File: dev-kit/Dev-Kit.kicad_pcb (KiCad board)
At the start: 4 copper layers, 105 x 70 mm, 110 parts, among them IC101 nPM1300-QEXX, IC107 USBLC6-2P6, IC201 APDS-9306-065, IC202 BMI270, IC203 BMP581, IC204 LIS2MDLTR, IC302 FAN5622SX, IC303 MX25U51245GZ4I00, IC305 NTS0104GU12, IC306 DRV2603RUNT, IC307 RV-8263-C8, M301 NORA-B106, Q201 DMG1013UW-7, Q301 BC817W, Q302 PMZ550UNEYL, Q303 PMZ550UNEYL, U201 MAX98357A, X101 Battery, X102 Motor, X103 Device, X104 DEBUG, X201 Power, X202 Power, X203 Power, X204 Power, X205 Power, X206 Power, X207 Power, X208 Power, X209 LED Power, X210 Touch Power, X211 IO Power, X302 Display

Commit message: Add CI/CD pipeline for Dev-Kit, more Dev-Kit improvements
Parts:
- removed BZ301: Buzzer, CUI Devices:CMT-322-65-SMT-TR
- removed D301: BAS316, Diode_SMD:D_SOD-323
- removed Q301: BC817W, Package_TO_SOT_SMD:SOT-323_SC-70
- removed R121: 0R, Resistor_SMD:R_0805_2012Metric
- removed R307: 150k, Resistor_SMD:R_0603_1608Metric
- removed R311: 180R, Resistor_SMD:R_0603_1608Metric
- removed TP104: SDA, TestPoint:TestPoint_Pad_D1.0mm
- removed TP105: SCL, TestPoint:TestPoint_Pad_D1.0mm
- removed U201: MAX98357A, Package_DFN_QFN:TQFN-16-1EP_3x3mm_P0.5mm_EP1.23x1.23mm
- added G***: LOGO, footprints:Logo, F.Cu at (156.8, 120.7)
- added X212: Power, Connector_PinHeader_2.54mm:PinHeader_1x02_P2.54mm_Vertical_SMD_Pin1Left, F.Cu at (158.0, 82.4)
- added X213: I2C, Connector_PinHeader_2.54mm:PinHeader_1x04_P2.54mm_Vertical_SMD_Pin1Left, F.Cu at (151.6, 139.2)
- added X214: I2S, Connector_PinHeader_2.54mm:PinHeader_1x05_P2.54mm_Vertical_SMD_Pin1Left, F.Cu at (139.7, 138.0)
- moved S301 60.8 mm to (148.0, 83.0), turned to 0 degrees
- moved S302 56.6 mm to (148.0, 128.0), turned to 0 degrees
- moved S304 53.2 mm to (123.0, 83.0), turned to 0 degrees
- moved X209 40.6 mm to (154.4, 112.7), turned to -90 degrees
- moved X210 39.0 mm to (152.2, 92.1)
- moved X211 38.9 mm to (158.6, 92.1), turned to -90 degrees
- moved S303 31.1 mm to (123.0, 129.0), turned to 0 degrees
- moved C301 29.3 mm to (165.1, 107.5)
- moved R301 29.3 mm to (165.1, 108.5)
- moved IC302 29.3 mm to (162.6, 108.1)
- moved R126 29.3 mm to (164.6, 105.1)
- moved R117 26.5 mm to (161.2, 101.2)
- moved R118 26.5 mm to (157.3, 101.2)
- moved C304 26.5 mm to (160.5, 99.7)
- moved C305 26.5 mm to (158.1, 99.7)
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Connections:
- M301 pad F7: unconnected-(M301C-P1.07-PadF7) -> /MCU/MCLK
- M301 pad G1: /MCU/SW3 -> /MCU/SW2
- M301 pad G2: /MCU/SW2 -> /MCU/SW4
- M301 pad G7: unconnected-(M301C-P1.09-PadG7) -> /MCU/WS
- M301 pad H1: /MCU/SW4 -> /MCU/SW3
- M301 pad J7: unconnected-(M301C-P1.10-PadJ7) -> /MCU/Data
- X211 pad 1: Net-(X211-Pin_1) -> +1V8
- X211 pad 2: +1V8 -> Net-(X211-Pin_2)
- X302 pad 11: Net-(X211-Pin_1) -> Net-(X211-Pin_2)
- X302 pad 12: Net-(X211-Pin_1) -> Net-(X211-Pin_2)
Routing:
- net /MCU/WS: track 0.00 -> 90.1 mm, vias 0 -> 3
- net /MCU/Data: track 0.00 -> 89.7 mm, vias 0 -> 3
- net /MCU/MCLK: track 0.00 -> 81.6 mm, vias 0 -> 3
- net /MCU/SW4: track 106.7 -> 151.3 mm, vias 1 -> 2
- net Net-(X211-Pin_2): track 0.00 -> 44.5 mm
- net Net-(X210-Pin_2): track 10.4 -> 48.9 mm
- net Net-(X209-Pin_2): track 3.24 -> 40.5 mm
- net /MCU/SW2: track 104.3 -> 72.1 mm, vias 1 -> 2
- net LEDK2: track 14.3 -> 43.5 mm
- net LEDK1: track 12.8 -> 42.1 mm
- net DISPLAY-BLK: track 76.2 -> 46.9 mm
- net TOUCH-RST: track 78.7 -> 51.8 mm
- net TOUCH-SDA: track 78.6 -> 51.8 mm
- net TOUCH-SCL: track 78.5 -> 51.9 mm
- net Net-(IC305-B4): track 17.8 -> 44.3 mm
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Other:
- board text added: "+"
- board text added: "-"
- board text added: "Display"

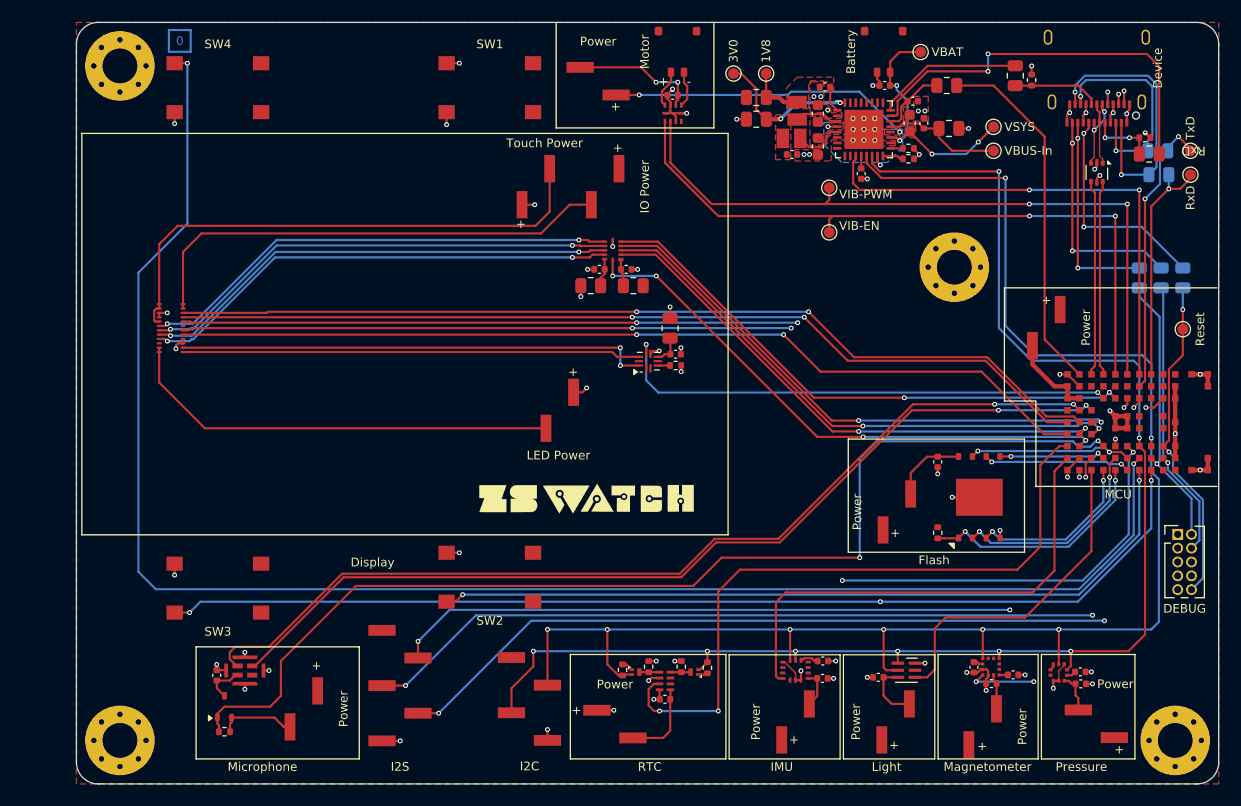
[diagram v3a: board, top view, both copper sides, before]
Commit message: PCB: Tweak silkscreen and headers.
- Added silkscreen labels to headers.
- Added function text to buttons.
- Made PCB 5mm wider (left) to make space for display (not sticking out of PCB) and allow more centered
buttons placement.
- Add header for UART pins (good in case we don't have a working dock built) (no mount).
- Changed from TP to header for VBAT for alternative way to connect battery (no mount).
- Added website url on silkscreen.
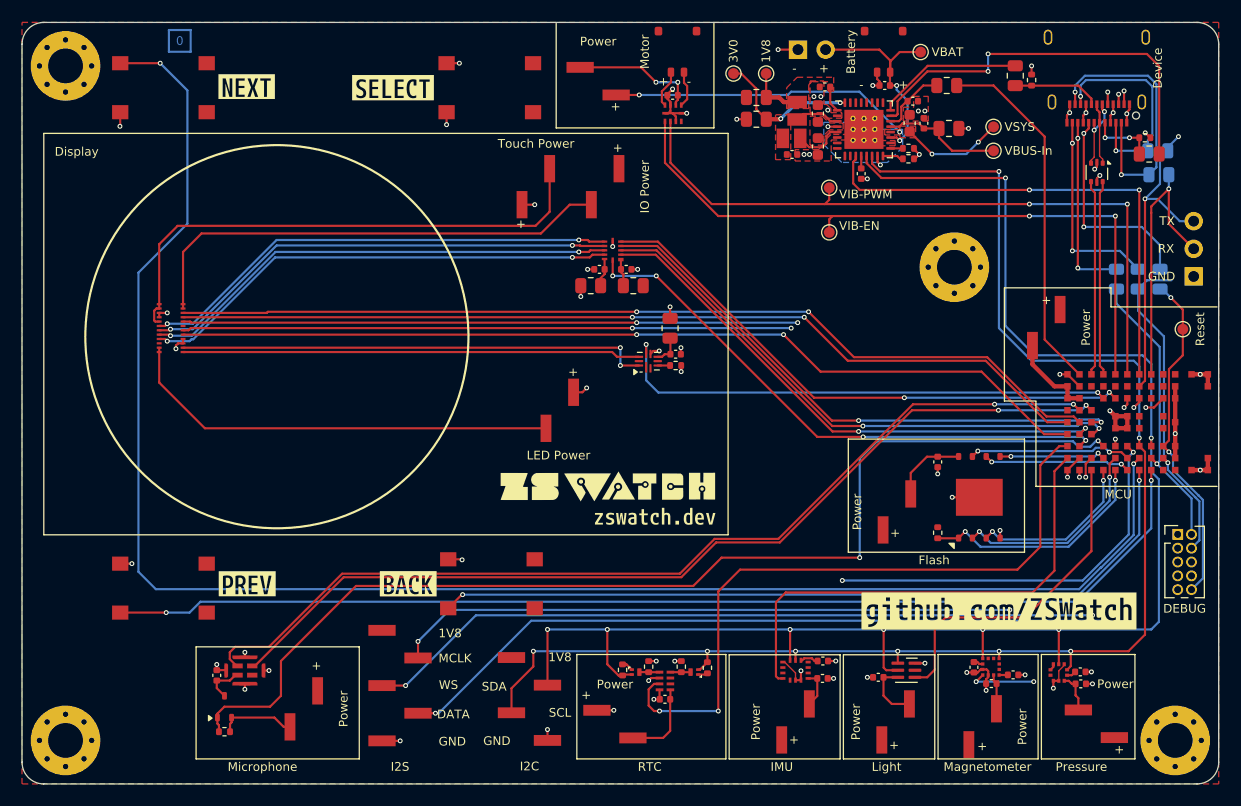
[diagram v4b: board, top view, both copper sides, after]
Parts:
- removed TP108: TxD, TestPoint:TestPoint_Pad_D1.0mm
- removed TP109: RxD, TestPoint:TestPoint_Pad_D1.0mm
- added J1: UART, Connector_PinHeader_2.54mm:PinHeader_1x03_P2.54mm_Vertical, F.Cu at (212.7, 95.3)
- added X1: Battery, Connector_PinHeader_2.54mm:PinHeader_1x02_P2.54mm_Vertical, F.Cu at (176.3, 79.5)
- added kibuzzard-68303879: G***, kibuzzard-68303879, F.Cu at (194.8, 131.1)
- added kibuzzard-68304278: G***, kibuzzard-68304278, F.Cu at (125.7, 128.6)
- added kibuzzard-68304289: G***, kibuzzard-68304289, F.Cu at (140.5, 128.6)
- added kibuzzard-6830428E: G***, kibuzzard-6830428E, F.Cu at (139.1, 83.0)
- added kibuzzard-68304292: G***, kibuzzard-68304292, F.Cu at (125.7, 82.9)
- added kibuzzard-68304463: G***, kibuzzard-68304463, F.Cu at (163.2, 122.4)
- moved REF** 5.00 mm to (109.0, 81.0)
- moved REF** 5.00 mm to (109.0, 143.0)
- moved S303 5.00 mm to (118.0, 129.0)
- moved S304 5.00 mm to (118.0, 83.0)
- moved G*** 2.26 mm to (158.8, 119.6)
- moved R106 2.10 mm to (205.6, 100.6)
- moved R107 2.10 mm to (207.6, 100.6)
- moved R130 2.10 mm to (209.6, 100.6)
- moved S302 0.62 mm to (148.2, 128.6)
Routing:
- net /Peripherals/VBAT: track 15.6 -> 23.0 mm
- net /MCU/SW3: track 139.4 -> 144.4 mm
- net SWDCLK: track 26.3 -> 31.0 mm
- net RxD: track 22.1 -> 25.8 mm
- net TxD: track 26.2 -> 29.9 mm
- net /MCU/SW4: track 151.3 -> 154.8 mm
- net GND: track 74.5 -> 76.7 mm, vias 57 -> 58
- net Net-(X103-RX1+): track 38.2 -> 36.1 mm
- net Net-(X103-RX1-): track 35.0 -> 33.0 mm
- net Net-(X103-SBU1): track 34.8 -> 34.0 mm
- net SWDIO: track 25.6 -> 26.3 mm
- net RESETn: track 30.4 -> 31.1 mm
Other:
- board size 105 x 70 mm -> 110 x 70 mm
- board text added: "1V8"
- board text added: "DATA"
- board text added: "GND"
- board text added: "MCLK"
- board text added: "RX"
- board text added: "SCL"
- board text added: "SDA"
- board text added: "TX"
- board text added: "WS"

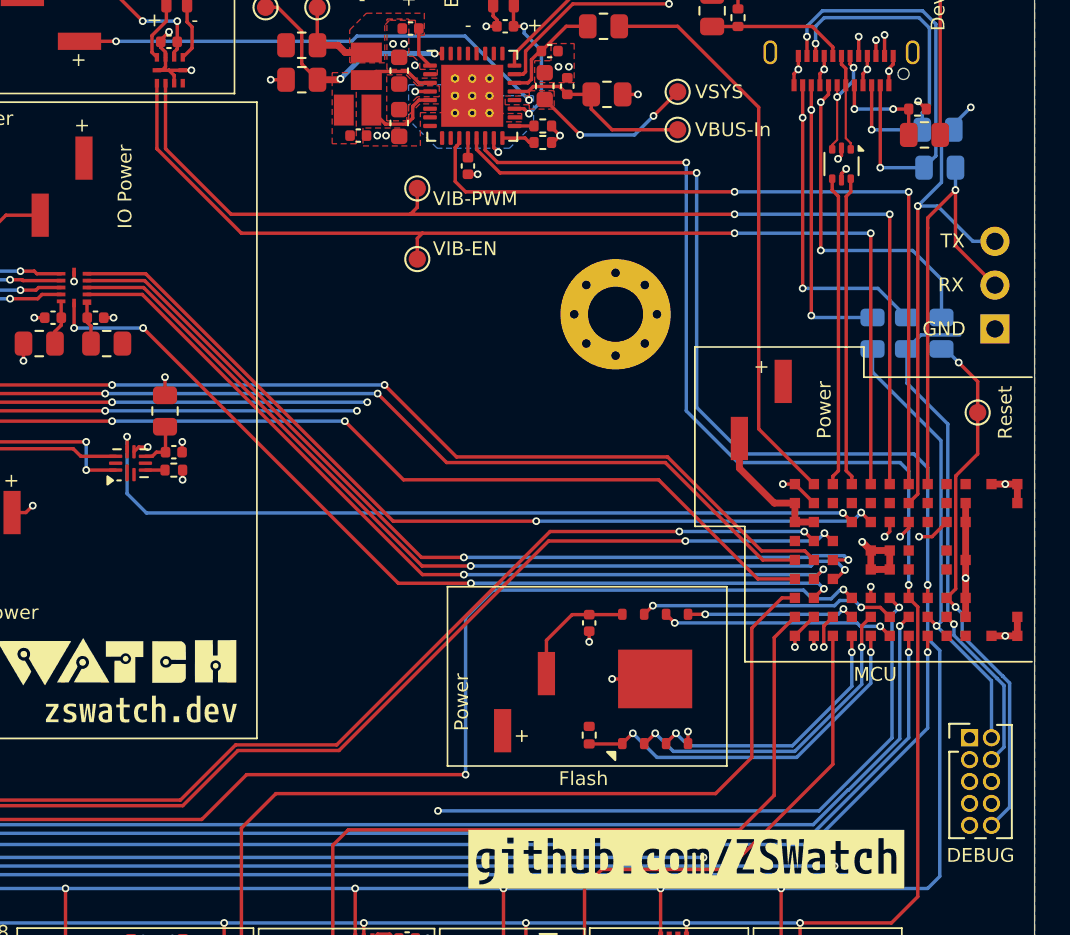
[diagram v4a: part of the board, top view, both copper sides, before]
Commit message: Fix wrong display SPI lines
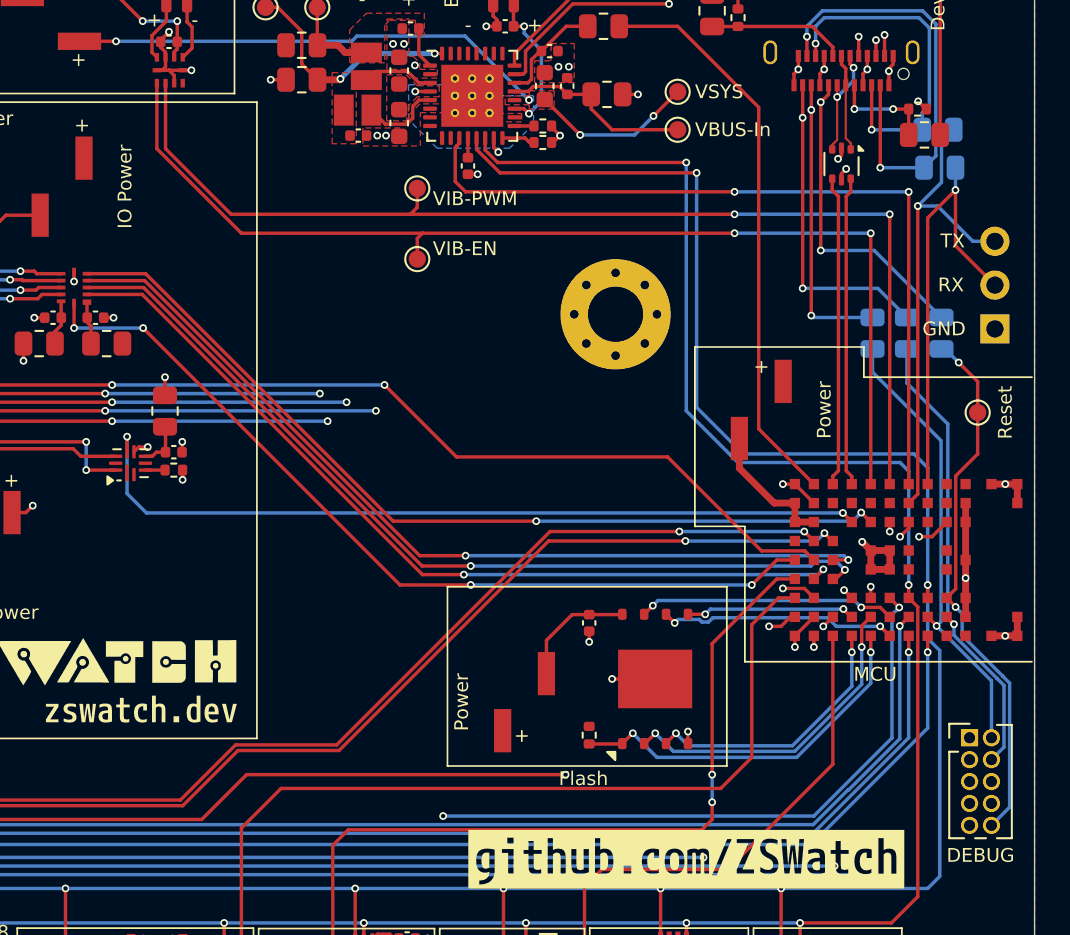
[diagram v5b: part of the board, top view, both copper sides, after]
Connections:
- M301 pad A2: /MCU/BMI270-INT -> DISPLAY-DC
- M301 pad A4: DISPLAY-DC -> /MCU/BMI270-INT
- M301 pad A5: DISPLAY-CS -> DISPLAY-EN
- M301 pad B1: DISPLAY-DATA -> DISPLAY-CLK
- M301 pad B3: DISPLAY-EN -> DISPLAY-CS
- M301 pad C2: DISPLAY-CLK -> DISPLAY-DATA
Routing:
- net /MCU/MIC-EN: track 101.4 -> 97.0 mm
- net SWDCLK: track 31.0 -> 27.7 mm
- net DISPLAY-DC: track 85.1 -> 87.9 mm, vias 2 -> 3
- net DISPLAY-CS: track 85.3 -> 87.6 mm, vias 2 -> 3
- net DISPLAY-EN: track 52.0 -> 50.0 mm
- net /MCU/BMI270-INT: track 45.2 -> 46.7 mm, vias 0 -> 2
- net TxD: track 29.9 -> 28.5 mm, vias 2 -> 1
- net Net-(X103-SBU1): track 34.0 -> 32.7 mm
- net DISPLAY-DATA: track 89.5 -> 90.3 mm
- net DISPLAY-CLK: track 91.5 -> 90.7 mm

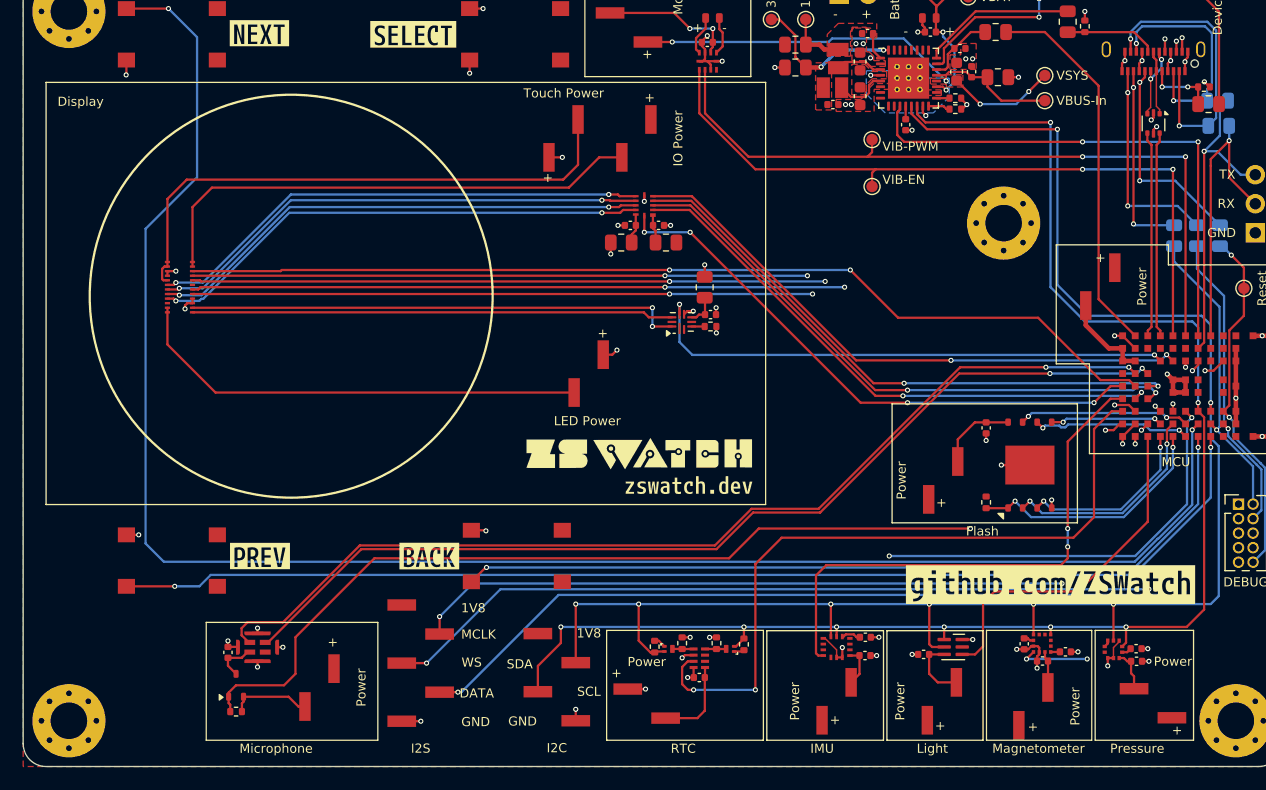
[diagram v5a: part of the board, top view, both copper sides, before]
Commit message: Add mounting holes for the display
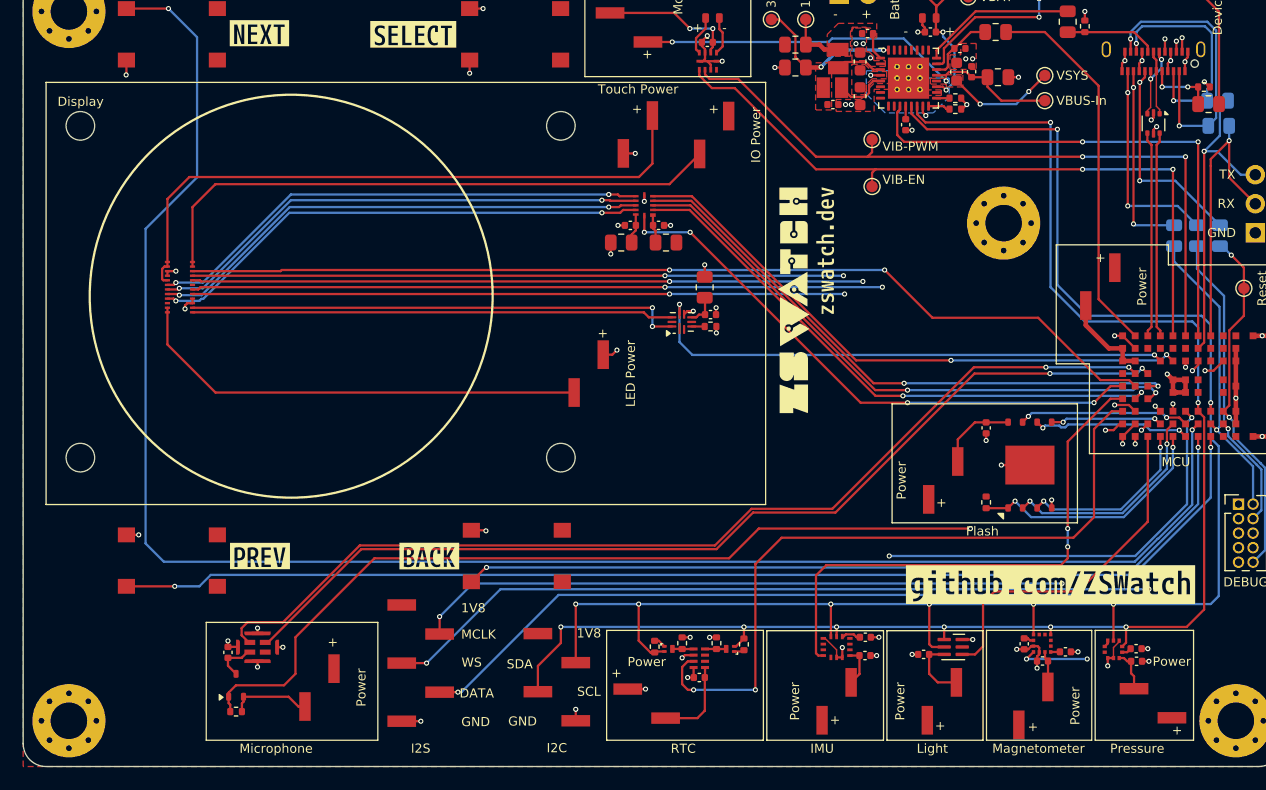
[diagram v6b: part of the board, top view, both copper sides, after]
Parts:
- added REF**: MountingHole_2.5mm, MountingHole:MountingHole_2.5mm, F.Cu at (152.0, 120.0)
- added REF**: MountingHole_2.5mm, MountingHole:MountingHole_2.5mm, F.Cu at (110.0, 120.0)
- added REF**: MountingHole_2.5mm, MountingHole:MountingHole_2.5mm, F.Cu at (152.0, 91.0)
- added REF**: MountingHole_2.5mm, MountingHole:MountingHole_2.5mm, F.Cu at (110.0, 91.0)
- moved kibuzzard-68304463 23.7 mm to (175.1, 101.9), turned to 90 degrees
- moved G*** 18.9 mm to (172.3, 106.3), turned to 90 degrees
- moved X211 6.81 mm to (165.4, 91.8)
- moved X210 6.51 mm to (158.7, 91.8)
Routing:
- net Net-(X211-Pin_2): track 44.5 -> 51.5 mm
- net Net-(X210-Pin_2): track 48.9 -> 55.7 mm
- net /MCU/VIB-PWM: track 64.7 -> 62.7 mm
- net /MCU/VIB-EN: track 63.4 -> 61.5 mm

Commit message: Changes from Jacob
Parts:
- removed C110: 1u, Capacitor_SMD:C_0402_1005Metric
- added C104: 1u, Capacitor_SMD:C_0402_1005Metric, F.Cu at (187.0, 84.3)
- added X103: Power, Connector_PinHeader_2.54mm:PinHeader_1x04_P2.54mm_Vertical, F.Cu at (116.9, 135.2)
- added X310: GPIO, Connector_PinHeader_2.54mm:PinHeader_1x06_P2.54mm_Vertical_SMD_Pin1Left, F.Cu at (174.1, 120.0)
- added kibuzzard-683075F5: G***, kibuzzard-683075F5, F.Cu at (140.4, 130.1)
- moved C203 5.66 mm to (173.2, 137.3), turned to 180 degrees
- moved kibuzzard-68304463 5.12 mm to (174.7, 96.8)
- moved G*** 5.12 mm to (171.9, 101.2)
- moved kibuzzard-68304289 1.20 mm to (140.5, 127.4)
- moved C101 0.10 mm to (188.0, 86.3)
- renumbered C104 to C106, C106 to C108, C204 to C202, C202 to C203, C307 to C204, C203 to C205, C208 to C206, C209 to C207, C211 to C208, C206 to C209, C207 to C210, C306 to C211, C304 to C303, C305 to C304, IC307 to IC202, IC202 to IC203, IC203 to IC205, IC306 to IC206, IC302 to IC301, IC303 to IC302, IC107 to IC303, IC305 to IC304, Q302 to Q202, Q303 to Q203, R119 to R103, R103 to R104, R108 to R105, R109 to R106, R304 to R202, R303 to R203, R313 to R204, R309 to R205, R126 to R303, R111 to R304, R112 to R305, R105 to R306, R104 to R307, R106 to R308, R107 to R309, R128 to R310, R129 to R311, R130 to R312, R117 to R313, R118 to R314, S301 to S201, S302 to S202, S303 to S203, S304 to S204, TP103 to TP101, TP107 to TP102, TP101 to TP103, TP102 to TP104, TP106 to TP105, TP112 to TP201, TP111 to TP202, TP110 to TP301, X1 to X101, X101 to X102, X204 to X201, X214 to X202, X201 to X203, X213 to X204, X206 to X205, X205 to X206, X203 to X207, X202 to X208, X212 to X209, X102 to X210, X207 to X301, X208 to X302, X103 to X303, J1 to X304, X211 to X305, X302 to X306, X210 to X307, X209 to X308, X104 to X309
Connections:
- IC101 pad 15: /MCU/SW3 -> /MCU/SW2
- IC303 pad 4: USB-D+ -> USB-D-
- IC303 pad 6: USB-D- -> USB-D+
- M301 pad C8: unconnected-(M301B-P0.22-PadC8) -> Net-(M301B-P0.22)
- M301 pad D8: unconnected-(M301B-P0.04/AIN0-PadD8) -> Net-(M301B-P0.04/AIN0)
- M301 pad E8: unconnected-(M301B-P0.05/AIN1-PadE8) -> Net-(M301B-P0.05/AIN1)
- M301 pad F8: unconnected-(M301C-P1.14-PadF8) -> Net-(M301C-P1.14)
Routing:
- net /Peripherals/VSYS: track 38.2 -> 137.1 mm
- net +3V0: track 5.34 -> 70.0 mm, vias 5 -> 7
- net /MCU/SW3: track 144.4 -> 103.3 mm, vias 4 -> 2
- net /MCU/SW2: track 72.2 -> 113.2 mm, vias 2 -> 4
- net Net-(M301C-P1.14): track 0.00 -> 40.9 mm, vias 0 -> 3
- net Net-(M301B-P0.04/AIN0): track 0.00 -> 38.1 mm, vias 0 -> 3
- net Net-(M301B-P0.22): track 0.00 -> 35.2 mm, vias 0 -> 3
- net Net-(M301B-P0.05/AIN1): track 0.00 -> 32.6 mm, vias 0 -> 3
- net /MCU/SDA: track 148.3 -> 146.1 mm
- net /MCU/SCL: track 136.3 -> 134.3 mm
- net +1V8: track 7.10 -> 8.50 mm
- net USB-D-: track 18.0 -> 19.0 mm, vias 0 -> 2
- net GND: track 76.7 -> 77.8 mm, vias 58 -> 59
- net /MCU/SW1: track 117.1 -> 116.5 mm
- net SWDCLK: track 27.7 -> 27.0 mm
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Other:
- board text removed: "RX"
- board text removed: "TX"
